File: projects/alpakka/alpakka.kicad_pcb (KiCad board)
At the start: 2 copper layers, 130 x 51 mm, 84 parts, among them P1 Conn_01x20_Pin, P2 Conn_01x20_Pin, P3 Headers 4P IN, P4 Blade, P6 Conn_01x02, U1 Alpsalpine_RKJXV, U10 ST_LSM6, U12 ST_LSM6, U2 Alpsalpine_RKJXV, U3 Alpsalpine_EC10E, U6 NXP_PCAL6416A, U8 NXP_PCAL6416A

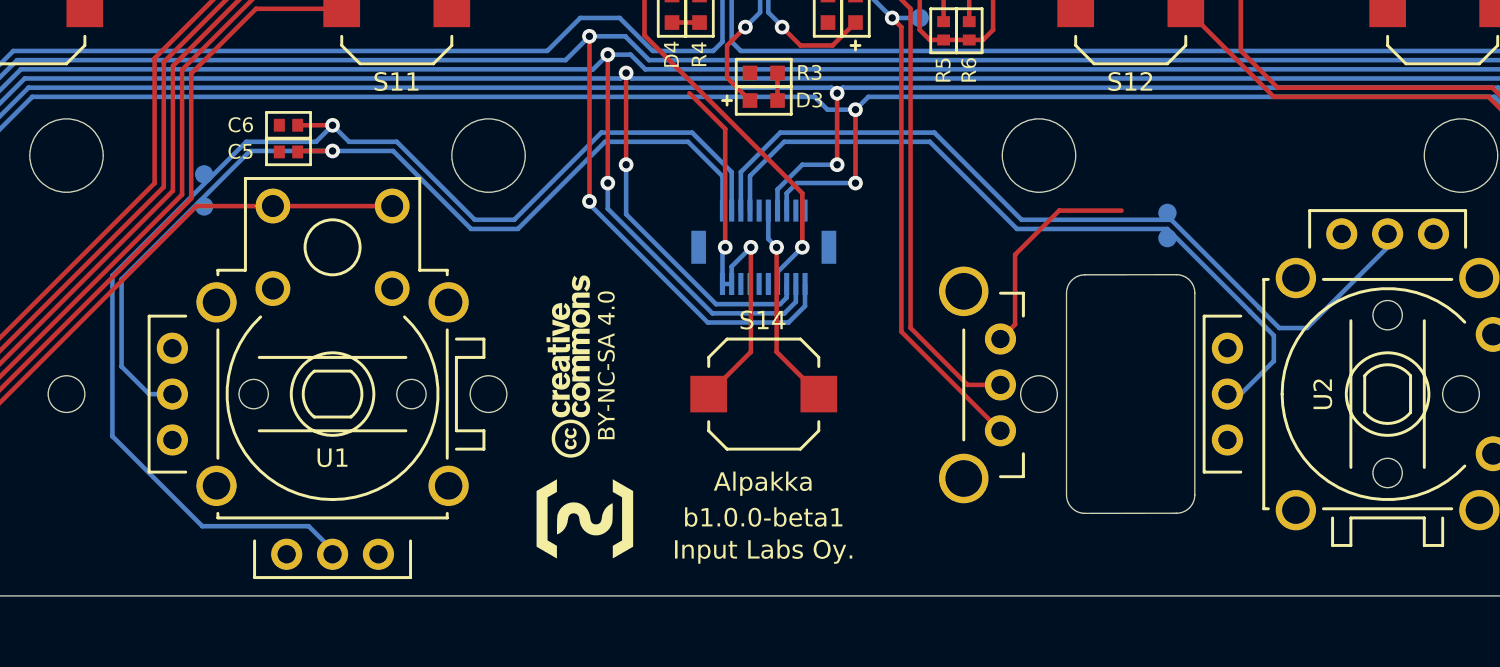
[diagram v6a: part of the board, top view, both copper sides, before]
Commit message: Thumbsticks without far caps, Thumbstick test points, Scrollwheel support dedicated holes
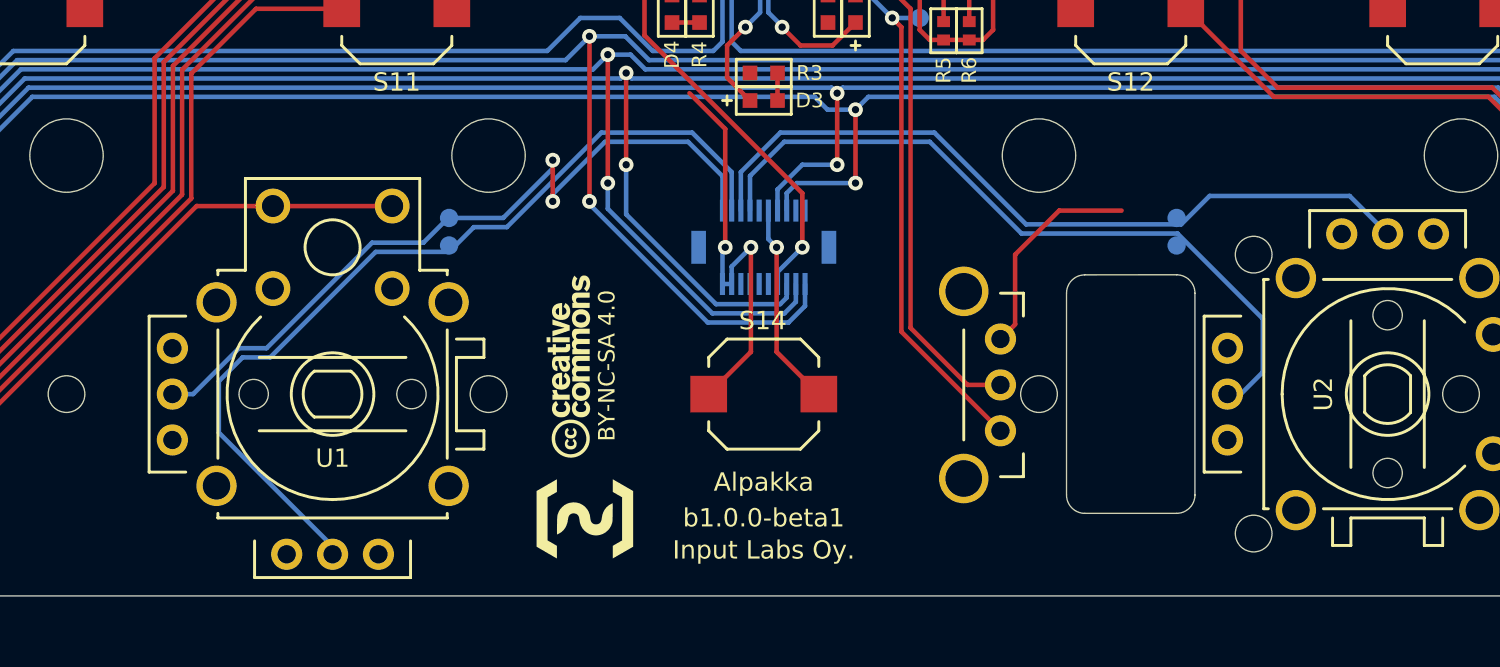
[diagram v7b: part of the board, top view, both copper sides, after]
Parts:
- removed C5, C6: 1uF, ILO_fp:0402
- added REF**: NPTH_2mm, ILO_fp:NPTH_2mm, F.Cu at (126.7, 82.6)
- added REF**: NPTH_2mm, ILO_fp:NPTH_2mm, F.Cu at (126.7, 67.4)
- moved TPA2 13.9 mm to (82.8, 66.9), turned to 0 degrees
- moved TPA3 13.4 mm to (82.8, 65.4), turned to 0 degrees
- moved TPA0 0.64 mm to (122.5, 66.9)
- moved TPA1 0.57 mm to (122.5, 65.4)
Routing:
- net /ADC2: track 69.7 -> 48.6 mm, vias 1 -> 0
- net /ADC3: track 52.2 -> 42.0 mm, vias 1 -> 2
- net /ADC1: track 45.2 -> 41.8 mm

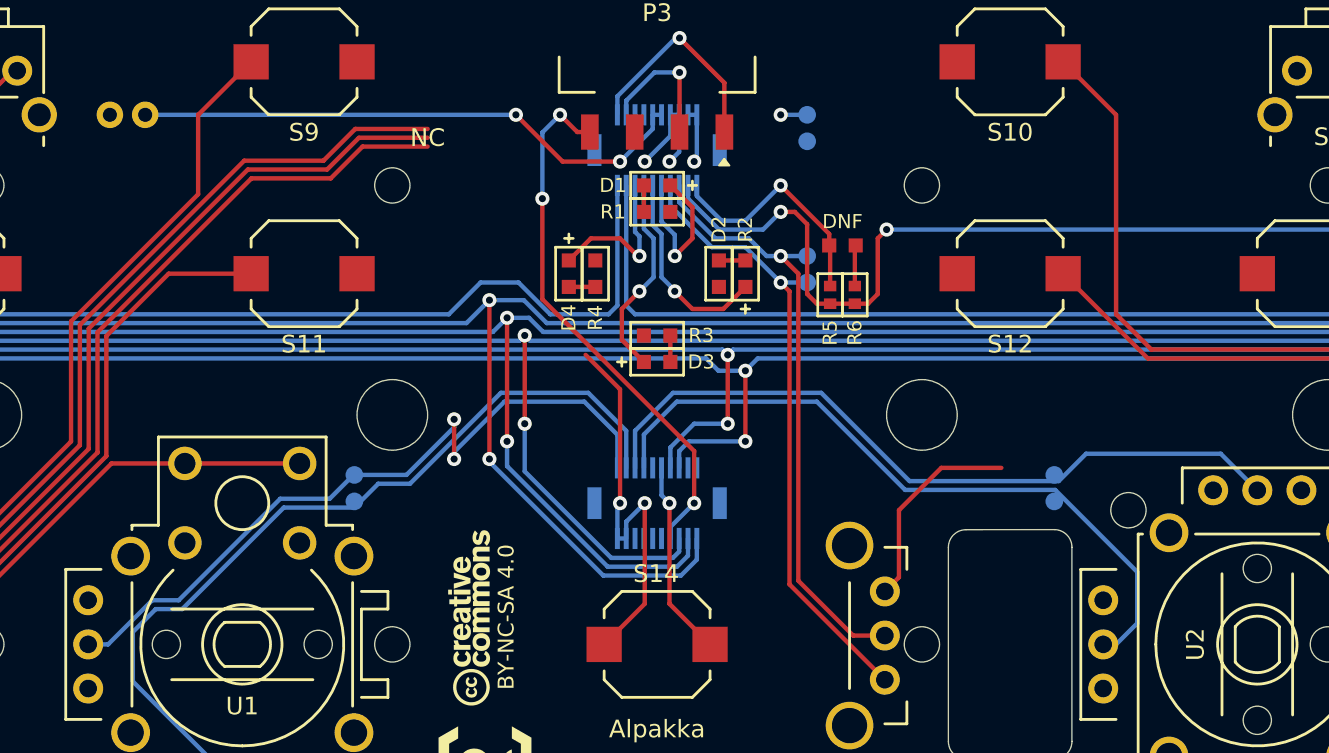
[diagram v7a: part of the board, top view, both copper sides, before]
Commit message: Added battery test point, Layout tweaks
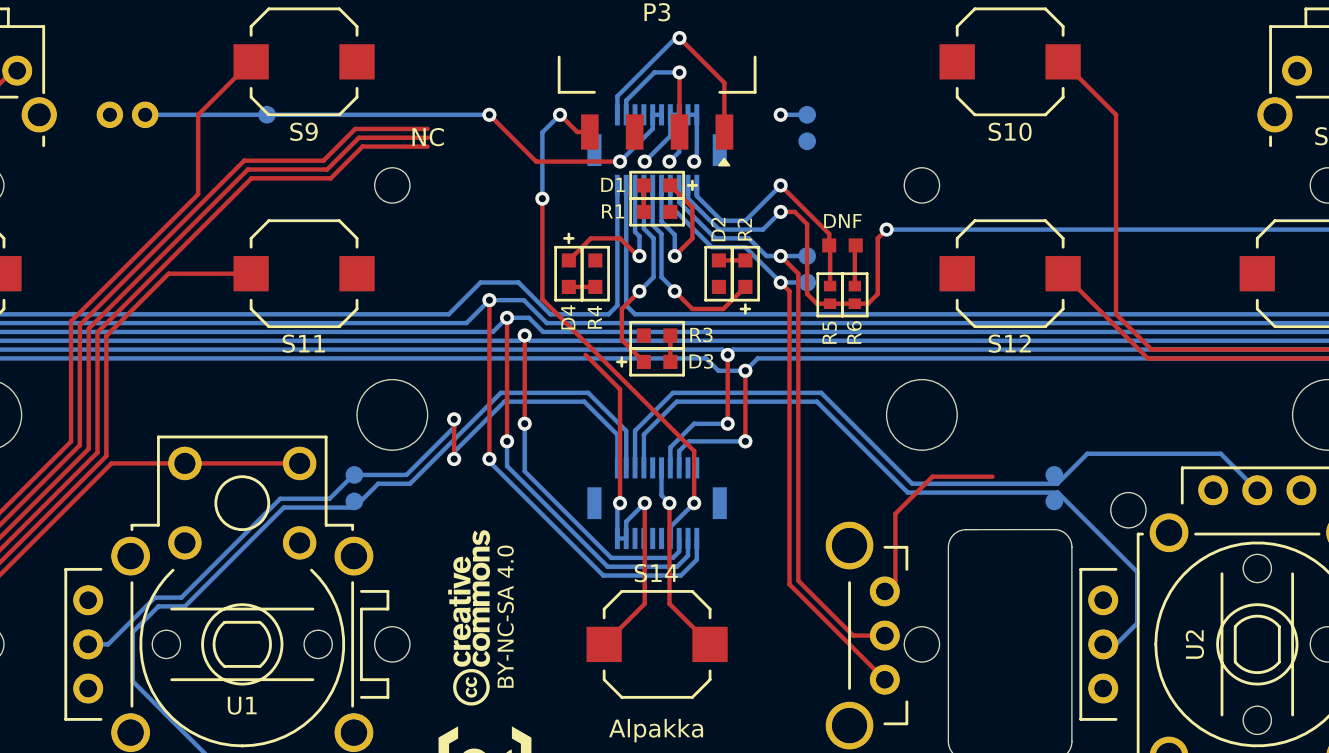
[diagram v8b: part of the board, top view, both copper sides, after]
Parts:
- added TPBAT0: Endpoint, ILO_fp:Pad_1mm, B.Cu at (77.9, 45.0)
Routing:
- net /GND: track 97.2 -> 96.5 mm
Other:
- board text added: "BAT"
- board text added: "GND"
- board text added: "VCC"
